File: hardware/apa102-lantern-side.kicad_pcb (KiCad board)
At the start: 2 copper layers, 25.4 x 109.2 mm, 11 parts, among them P1 CONN_6, P2 CONN_6, U1 APA102, U2 APA102, U3 APA102, U4 APA102, U5 APA102, U6 APA102, U7 APA102, U8 APA102

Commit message: Adds github url to pcbs
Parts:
- moved REF** 2.54 mm to (134.6, 133.3)
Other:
- board text added: "github.com/Nervengift/apa102lantern"
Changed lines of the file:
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@@
     (area 114.249999 81.229999 139.750001 190.550001)
     (thickness 1.6)
-    (drawings 12)
+    (drawings 13)
     (tracks 81)
     (zones 0)
@@
   )
   (module Symbols:Symbol_CreativeCommonsPublicDomain_SilkScreenTop_Small (layer B.Cu)
-    (at 134.62 130.81 270)
+    (at 134.62 133.35 270)
     (descr "Symbol, Creative Commons Public Domain, SilkScreenTop, Small,")
     (tags "Symbol, Creative Commons Public Domain, SilkScreen Top, Small,")
@@
     (fp_line (start -13.15056 2.3003) (end -13.75 2.39936) (layer B.SilkS) (width 0.15))
   )
+  (gr_text github.com/Nervengift/apa102lantern (at 118.11 134.62 90) (layer B.SilkS)
+    (effects (font (size 1.5 1.5) (thickness 0.3)) (justify mirror))
+  )
   (gr_text "led board" (at 134.62 166.37 90) (layer F.SilkS)

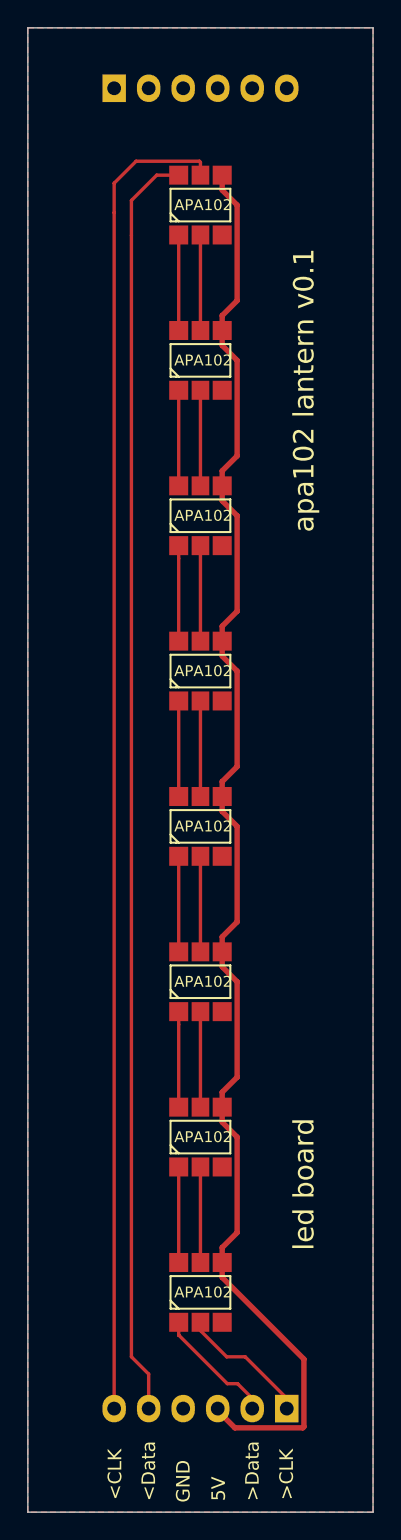
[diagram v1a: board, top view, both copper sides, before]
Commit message: Fix pin headers and add VCC on 2nd pin panel
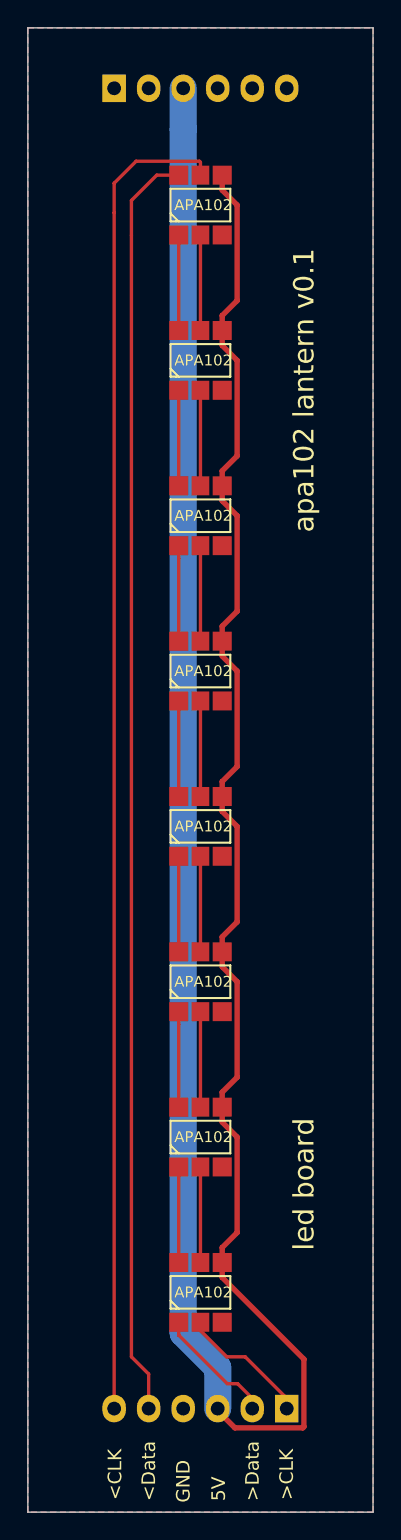
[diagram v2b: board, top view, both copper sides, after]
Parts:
- P1, P2: value CONN_6 -> CONN_01X06
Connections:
- P2 pad 3: Net-(P1-Pad4) -> Net-(P1-Pad3)
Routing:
- net Net-(P1-Pad3): track 108.0 -> 206.2 mm
- added copper zone on B.Cu, net Net-(P1-Pad4)
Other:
- net class vcc: trace_width 0.4 -> 2
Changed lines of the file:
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@@
   (general
     (links 40)
-    (no_connects 0)
+    (no_connects 1)
     (area 114.249999 81.229999 139.750001 190.550001)
     (thickness 1.6)
     (drawings 13)
-    (tracks 81)
+    (tracks 85)
     (zones 0)
     (modules 11)
@@
   (net_class vcc ""
     (clearance 0.2)
-    (trace_width 0.4)
+    (trace_width 2)
     (via_dia 0.6)
     (via_drill 0.4)
@@
       (effects (font (size 1 1) (thickness 0.15)) (justify mirror))
     )
-    (fp_text value CONN_6 (at 0 3.1 90) (layer B.Fab)
+    (fp_text value CONN_01X06 (at 0 3.1 90) (layer B.Fab)
       (effects (font (size 1 1) (thickness 0.15)) (justify mirror))
     )
@@
       (effects (font (size 1 1) (thickness 0.15)) (justify mirror))
     )
-    (fp_text value CONN_6 (at 0 3.1 270) (layer B.Fab)
+    (fp_text value CONN_01X06 (at 0 3.1 270) (layer B.Fab)
       (effects (font (size 1 1) (thickness 0.15)) (justify mirror))
     )
@@
       (net 4 "Net-(P1-Pad4)"))
     (pad 3 thru_hole oval (at 0 -5.08 270) (size 2.032 1.7272) (drill 1.016) (layers *.Cu *.Mask B.SilkS)
-      (net 4 "Net-(P1-Pad4)"))
+      (net 3 "Net-(P1-Pad3)"))
     (pad 4 thru_hole oval (at 0 -7.62 270) (size 2.032 1.7272) (drill 1.016) (layers *.Cu *.Mask B.SilkS)
       (net 4 "Net-(P1-Pad4)"))
@@
   (segment (start 125.4 177.47) (end 128.9775 181.0475) (width 0.25) (layer F.Cu) (net 2))
   (segment (start 129.73188 181.0475) (end 130.81 182.12562) (width 0.25) (layer F.Cu) (net 2))
+  (segment (start 128.27 182.88) (end 128.27 179.864) (width 2) (layer B.Cu) (net 3))
+  (segment (start 128.27 179.864) (end 125.73 177.324) (width 2) (layer B.Cu) (net 3))
+  (segment (start 125.73 177.324) (end 125.73 88.741) (width 2) (layer B.Cu) (net 3))
+  (segment (start 125.73 88.741) (end 125.73 85.725) (width 2) (layer B.Cu) (net 3))
   (segment (start 128.6 103.55) (end 128.6 102.45) (width 0.4) (layer F.Cu) (net 3))
   (segment (start 128.6 102.45) (end 129.700001 101.349999) (width 0.4) (layer F.Cu) (net 3))
@@
       )
     )
+  )
+  (zone (net 4) (net_name "Net-(P1-Pad4)") (layer B.Cu) (hatch edge 0.508)
+    (connect_pads (clearance 0.508))
+    (min_thickness 0.254)
+    (fill yes (arc_segments 16) (thermal_gap 0.508) (thermal_bridge_width 0.508))
+    (polygon
+      (pts
+        (xy 114.3 81.28) (xy 139.7 81.28) (xy 139.7 190.5) (xy 114.3 190.5)
+      )
+    )

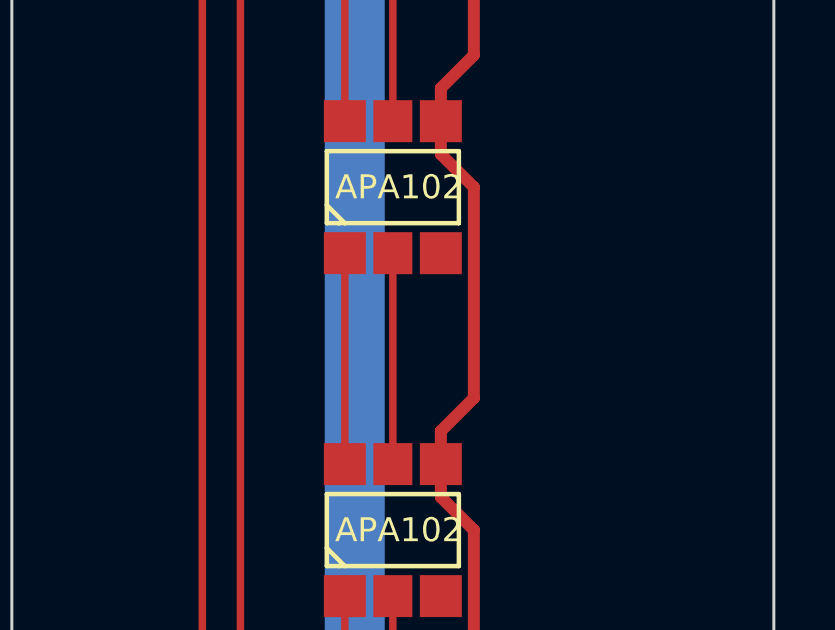
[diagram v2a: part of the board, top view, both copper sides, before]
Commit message: Adds a capacitor on the led board (just to be sure)
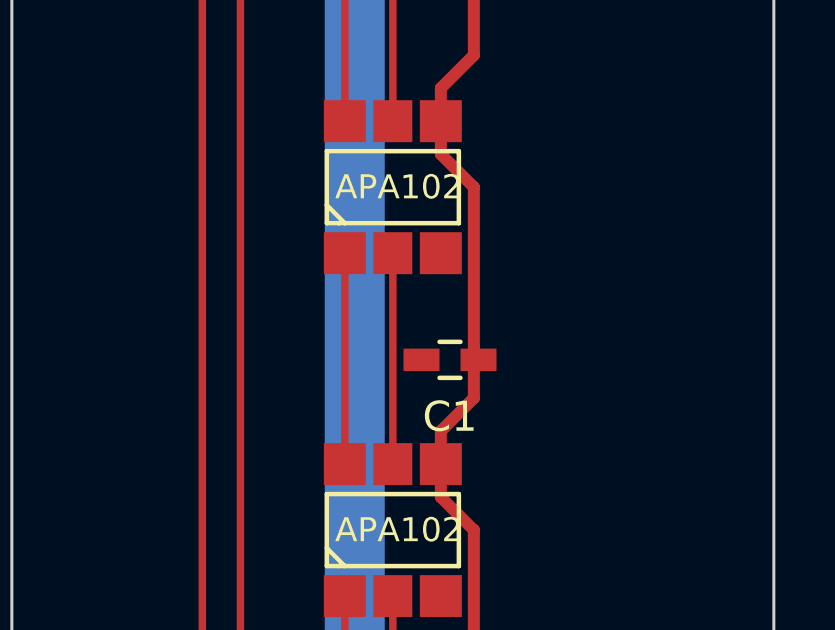
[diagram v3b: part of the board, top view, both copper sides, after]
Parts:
- added C1: 0.1u, Capacitors_SMD:C_0603_HandSoldering, F.Cu at (128.9, 134.4)
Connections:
- net Net-(P1-Pad1) renamed />clk
- net Net-(P1-Pad2) renamed />D
- net Net-(P1-Pad3) renamed /5V
- net Net-(P1-Pad4) renamed /GND
- net Net-(P1-Pad5) renamed /D>
- net Net-(P1-Pad6) renamed /clk>
